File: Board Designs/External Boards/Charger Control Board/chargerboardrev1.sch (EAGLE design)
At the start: 17 parts, among them X1 CONNECTOR-6NANO-FIT_VERTICAL-6, X3 CONNECTOR-2, X4 CONNECTOR-2

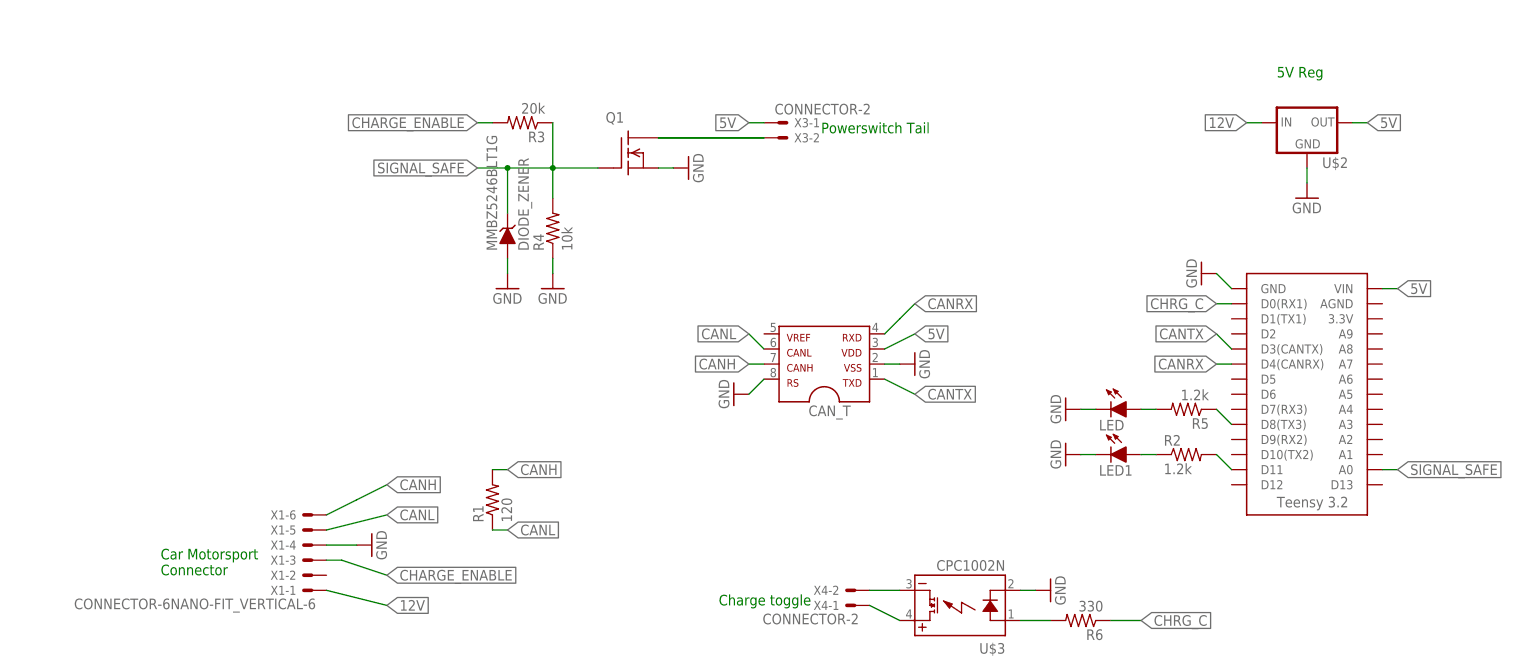
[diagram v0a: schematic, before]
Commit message: added jumper and added capacitor to 5v reg
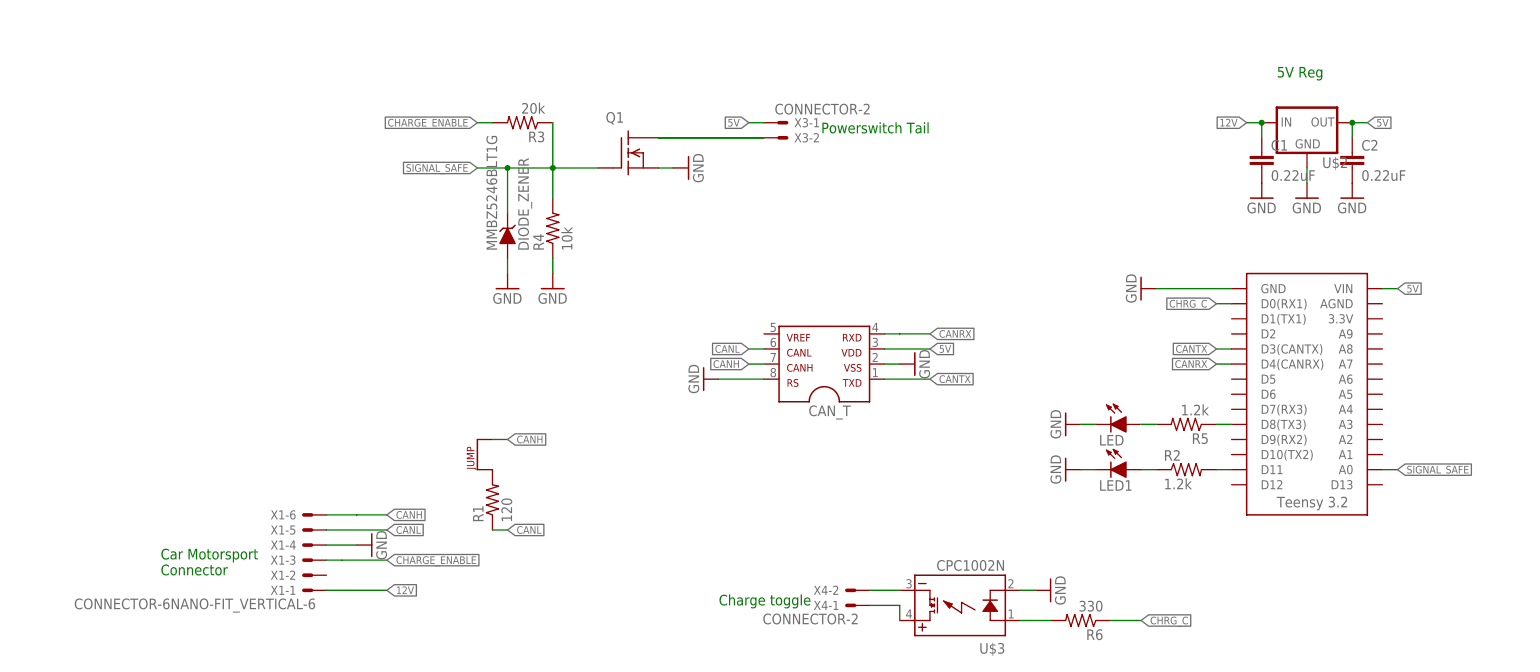
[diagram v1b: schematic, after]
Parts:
- added C1, C2: 0.22uF, HyTechDevices:CAP0805
- added J1: JUMPER.1, HyTechDevices:JUMPER.1
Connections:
- new net N$5: J1.P$1, R1.2
- net 12V: now also C1.1
- net 5V: now also C2.1
- net CANH: now also J1.P$2; no longer R1.2
- net GND: now also C1.2, C2.2
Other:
- moved on the sheet: LED, LED1, R2, R5

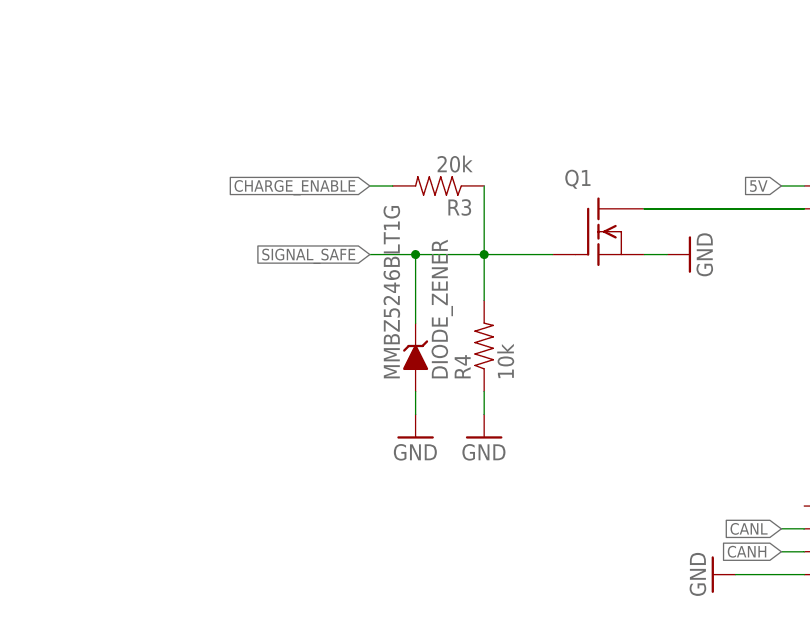
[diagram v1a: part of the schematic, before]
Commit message: Charger Control Board with suggested modifications
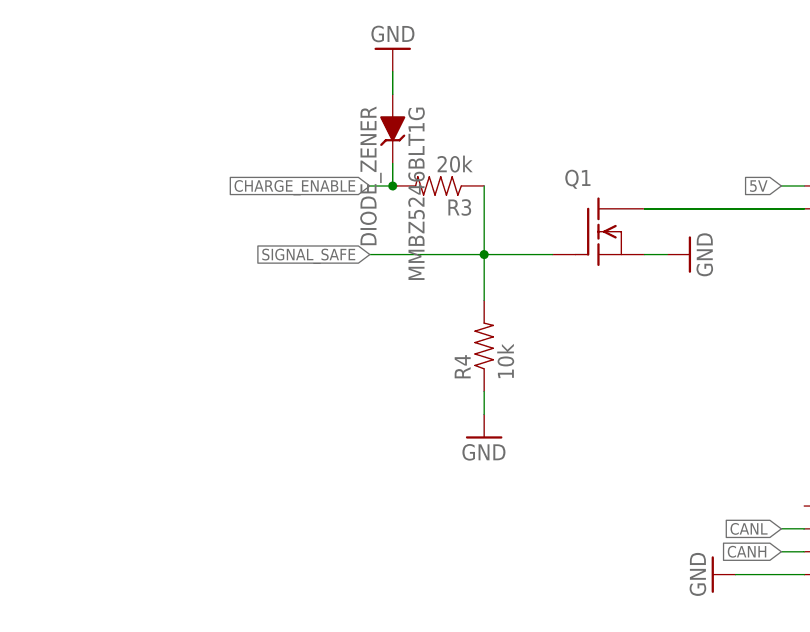
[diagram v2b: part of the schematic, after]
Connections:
- net CHARGE_ENABLE: now also MMBZ5246BLT1G.C
- net SIGNAL_SAFE: no longer MMBZ5246BLT1G.C
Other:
- moved on the sheet: MMBZ5246BLT1G
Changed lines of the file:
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@@
 <instance part="R4" gate="G$1" x="-114.3" y="68.58" rot="R90"/>
 <instance part="GND9" gate="1" x="-114.3" y="58.42"/>
-<instance part="MMBZ5246BLT1G" gate="G$1" x="-121.92" y="68.58" rot="R90"/>
-<instance part="GND8" gate="1" x="-121.92" y="58.42"/>
+<instance part="MMBZ5246BLT1G" gate="G$1" x="-124.46" y="91.44" rot="R270"/>
+<instance part="GND8" gate="1" x="-124.46" y="101.6" rot="R180"/>
 <instance part="Q1" gate="G$1" x="-101.6" y="81.28"/>
 <instance part="R2" gate="G$1" x="-7.62" y="27.94"/>
@@
 <segment>
 <pinref part="MMBZ5246BLT1G" gate="G$1" pin="A"/>
-<wire x1="-121.92" y1="63.5" x2="-121.92" y2="60.96" width="0.1524" layer="91"/>
+<wire x1="-124.46" y1="96.52" x2="-124.46" y2="99.06" width="0.1524" layer="91"/>
 <pinref part="GND8" gate="1" pin="GND"/>
 </segment>
@@
 <pinref part="R3" gate="G$1" pin="2"/>
 <label x="-127" y="86.36" size="1.27" layer="95" rot="R180" xref="yes"/>
+<pinref part="MMBZ5246BLT1G" gate="G$1" pin="C"/>
+<wire x1="-124.46" y1="86.36" x2="-124.46" y2="88.9" width="0.1524" layer="91"/>
+<junction x="-124.46" y="86.36"/>
 </segment>
 <segment>
@@
 <pinref part="Q1" gate="G$1" pin="G"/>
 <wire x1="-114.3" y1="78.74" x2="-121.92" y2="78.74" width="0.1524" layer="91"/>
-<pinref part="MMBZ5246BLT1G" gate="G$1" pin="C"/>
-<wire x1="-121.92" y1="78.74" x2="-121.92" y2="71.12" width="0.1524" layer="91"/>
 <wire x1="-121.92" y1="78.74" x2="-127" y2="78.74" width="0.1524" layer="91"/>
-<junction x="-121.92" y="78.74"/>
 <label x="-127" y="78.74" size="1.27" layer="95" rot="R180" xref="yes"/>
 </segment>

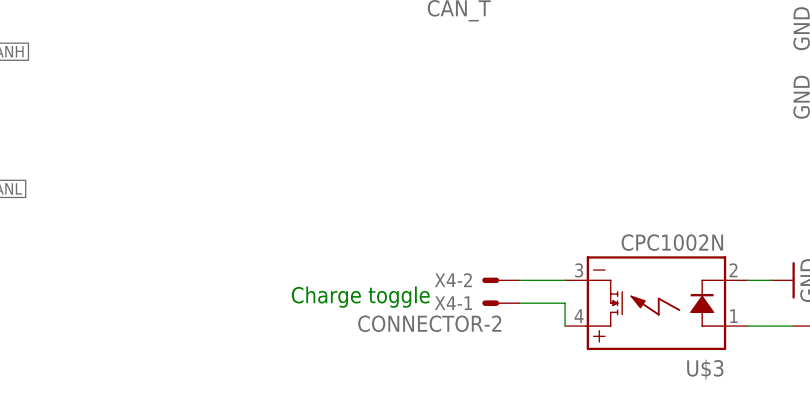
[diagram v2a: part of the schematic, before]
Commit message: Charger control board with modifications to control external relay board
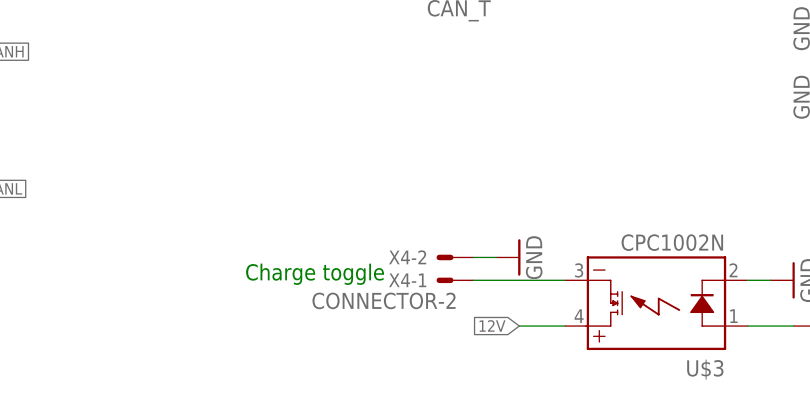
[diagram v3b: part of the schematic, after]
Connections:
- removed net N$8: U$3.DC+, X4-1.S
- net 12V: now also U$3.DC+
- net GND: now also X4-2.S
- net N$7: now also X4-1.S; no longer X4-2.S
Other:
- moved on the sheet: X4-1, X4-2
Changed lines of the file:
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@@
 <part name="GND13" library="HyTechSymbols" deviceset="GND" device=""/>
 <part name="J1" library="HyTechDevices" deviceset="JUMPER" device=".1"/>
+<part name="GND14" library="HyTechSymbols" deviceset="GND" device=""/>
 </parts>
 <sheets>
@@
 Connector</text>
 <text x="-50.8" y="86.36" size="1.778" layer="91" rot="R180">Powerswitch Tail</text>
-<text x="-86.36" y="5.08" size="1.778" layer="91">Charge toggle</text>
+<text x="-91.44" y="7.62" size="1.778" layer="91">Charge toggle</text>
 <text x="7.62" y="93.98" size="1.778" layer="91">5V Reg</text>
 </plain>
@@
 <instance part="R5" gate="G$1" x="-7.62" y="35.56" rot="R180"/>
 <instance part="GND11" gate="1" x="-27.94" y="35.56" rot="R270"/>
-<instance part="X4" gate="-2" x="-63.5" y="7.62" rot="R180"/>
-<instance part="X4" gate="-1" x="-63.5" y="5.08" rot="R180"/>
+<instance part="X4" gate="-2" x="-68.58" y="10.16" rot="R180"/>
+<instance part="X4" gate="-1" x="-68.58" y="7.62" rot="R180"/>
 <instance part="U$3" gate="G$1" x="-45.72" y="5.08" rot="R180"/>
 <instance part="GND12" gate="1" x="-30.48" y="7.62" rot="R90"/>
@@
 <instance part="GND13" gate="1" x="20.32" y="73.66"/>
 <instance part="J1" gate="G$1" x="-127" y="27.94" rot="R90"/>
+<instance part="GND14" gate="1" x="-60.96" y="10.16" rot="R90"/>
 </instances>
 <busses>
@@
 <pinref part="GND13" gate="1" pin="GND"/>
 </segment>
+<segment>
+<pinref part="X4" gate="-2" pin="S"/>
+<wire x1="-66.04" y1="10.16" x2="-63.5" y2="10.16" width="0.1524" layer="91"/>
+<pinref part="GND14" gate="1" pin="GND"/>
+</segment>
 </net>
 <net name="CANRX" class="0">
@@
 <label x="-142.24" y="7.62" size="1.27" layer="95" xref="yes"/>
 </segment>
+<segment>
+<pinref part="U$3" gate="G$1" pin="DC+"/>
+<wire x1="-55.88" y1="2.54" x2="-60.96" y2="2.54" width="0.1524" layer="91"/>
+<label x="-60.96" y="2.54" size="1.27" layer="95" rot="R180" xref="yes"/>
+</segment>
 </net>
 <net name="N$1" class="0">
@@
 <pinref part="LED" gate="LED" pin="A"/>
 <wire x1="-12.7" y1="35.56" x2="-15.24" y2="35.56" width="0.1524" layer="91"/>
-</segment>
-</net>
-<net name="N$7" class="0">
-<segment>
-<pinref part="U$3" gate="G$1" pin="DC-"/>
-<pinref part="X4" gate="-2" pin="S"/>
-<wire x1="-55.88" y1="7.62" x2="-60.96" y2="7.62" width="0.1524" layer="91"/>
-</segment>
-</net>
-<net name="N$8" class="0">
-<segment>
-<pinref part="X4" gate="-1" pin="S"/>
-<pinref part="U$3" gate="G$1" pin="DC+"/>
-<wire x1="-55.88" y1="2.54" x2="-55.88" y2="5.08" width="0.1524" layer="91"/>
-<wire x1="-55.88" y1="5.08" x2="-60.96" y2="5.08" width="0.1524" layer="91"/>
 </segment>
 </net>
@@
 </segment>
 </net>
+<net name="N$7" class="0">
+<segment>
+<pinref part="U$3" gate="G$1" pin="DC-"/>
+<pinref part="X4" gate="-1" pin="S"/>
+<wire x1="-55.88" y1="7.62" x2="-66.04" y2="7.62" width="0.1524" layer="91"/>
+</segment>
+</net>
